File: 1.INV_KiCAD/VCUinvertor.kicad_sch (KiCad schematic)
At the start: 119 parts, among them J7 PowerSupply, J9 BRAKE LIGHT, Q1 2N7002, Q10 2N7002, Q11 BC848C, Q12 BCP51, Q2 2N7002, Q3 2N7002, Q4 2N7002, Q5 2N7002, Q6 2N7002, Q7 2N7002, Q8 2N7002, Q9 2N7002, U1 TJA1448ATK, U2 REF3433T, U3 TLV76150DCY

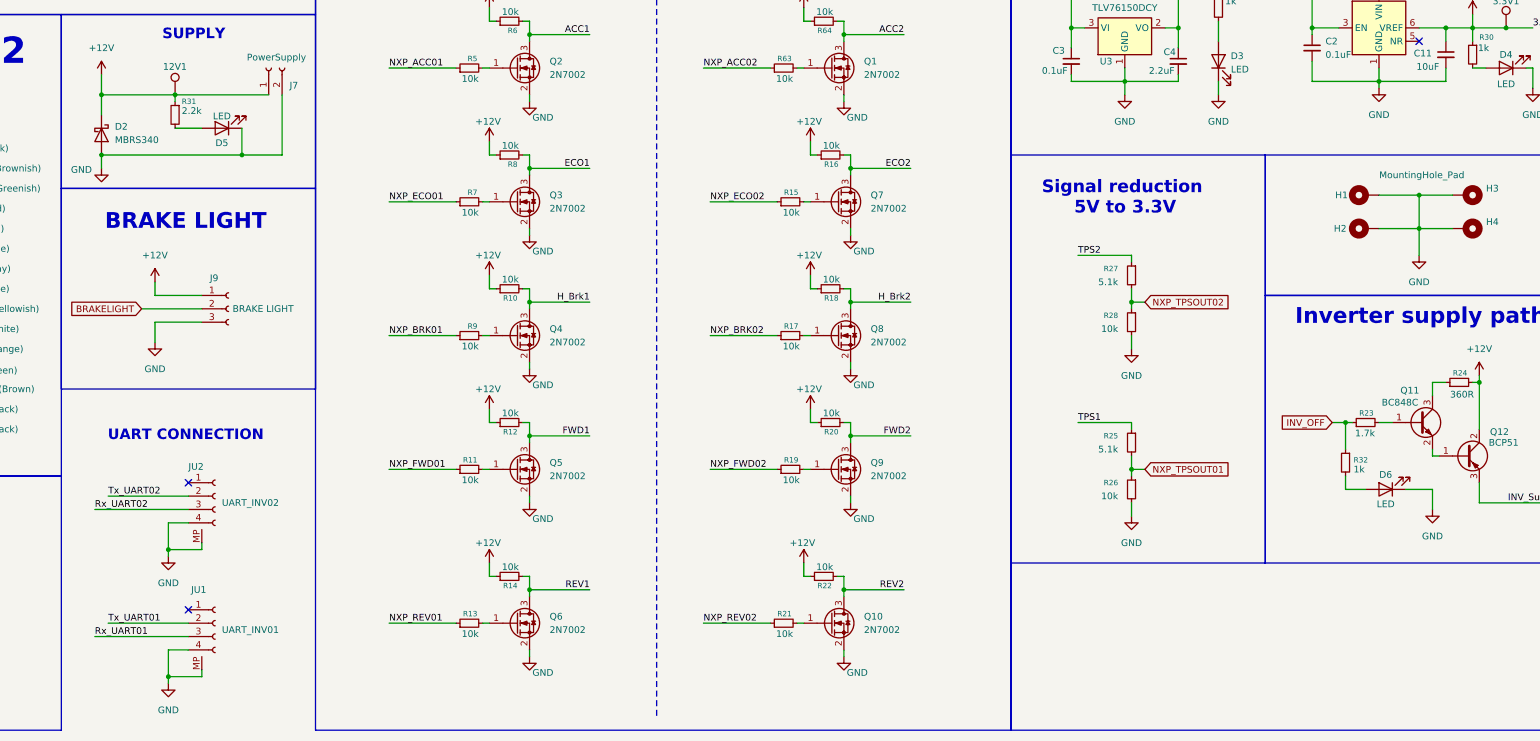
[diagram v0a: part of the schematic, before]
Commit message: Corrections on UART01/02
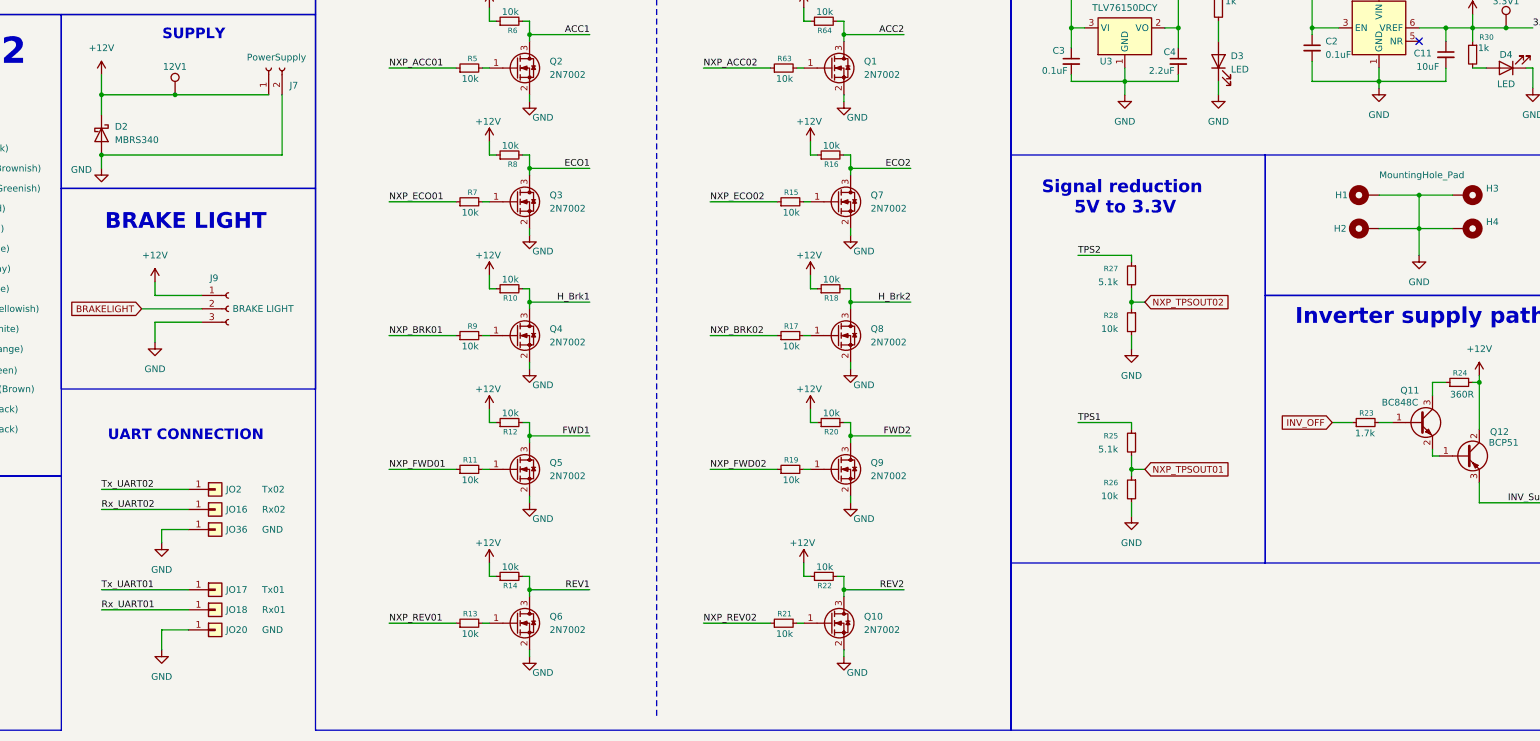
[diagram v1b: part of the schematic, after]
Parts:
- removed D5, D6: LED, LED_SMD:LED_0805_2012Metric_Pad1.15x1.40mm_HandSolder, symbol Device:LED
- removed JU1: UART_INV01, Connector_JST:JST_GH_SM04B-GHS-TB_1x04-1MP_P1.25mm_Horizontal, symbol Connector:Conn_01x04_Socket
- removed JU2: UART_INV02, Connector_JST:JST_GH_SM04B-GHS-TB_1x04-1MP_P1.25mm_Horizontal, symbol Connector:Conn_01x04_Socket
- removed R31: 2.2k, Resistor_SMD:R_0805_2012Metric, symbol Device:R_Small
- removed R32: 1k, Resistor_SMD:R_0805_2012Metric, symbol Device:R_Small
- added JO16: Rx02, Connector_Wire:SolderWire-0.5sqmm_1x01_D0.9mm_OD2.1mm, symbol Connector_Generic:Conn_01x01
- added JO17: Tx01, Connector_Wire:SolderWire-0.5sqmm_1x01_D0.9mm_OD2.1mm, symbol Connector_Generic:Conn_01x01
- added JO18: Rx01, Connector_Wire:SolderWire-0.5sqmm_1x01_D0.9mm_OD2.1mm, symbol Connector_Generic:Conn_01x01
- added JO2: Tx02, Connector_Wire:SolderWire-0.5sqmm_1x01_D0.9mm_OD2.1mm, symbol Connector_Generic:Conn_01x01
- added JO20, JO36: GND, Connector_Wire:SolderWire-0.5sqmm_1x01_D0.9mm_OD2.1mm, symbol Connector_Generic:Conn_01x01
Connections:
- net GND: now also JO20.1 (Pin_1), JO36.1 (Pin_1)
- net Rx_UART01: now also JO18.1 (Pin_1)
- net Rx_UART02: now also JO16.1 (Pin_1)
- net Tx_UART01: now also JO17.1 (Pin_1)
- net Tx_UART02: now also JO2.1 (Pin_1)
- no-connect marks 90 -> 88

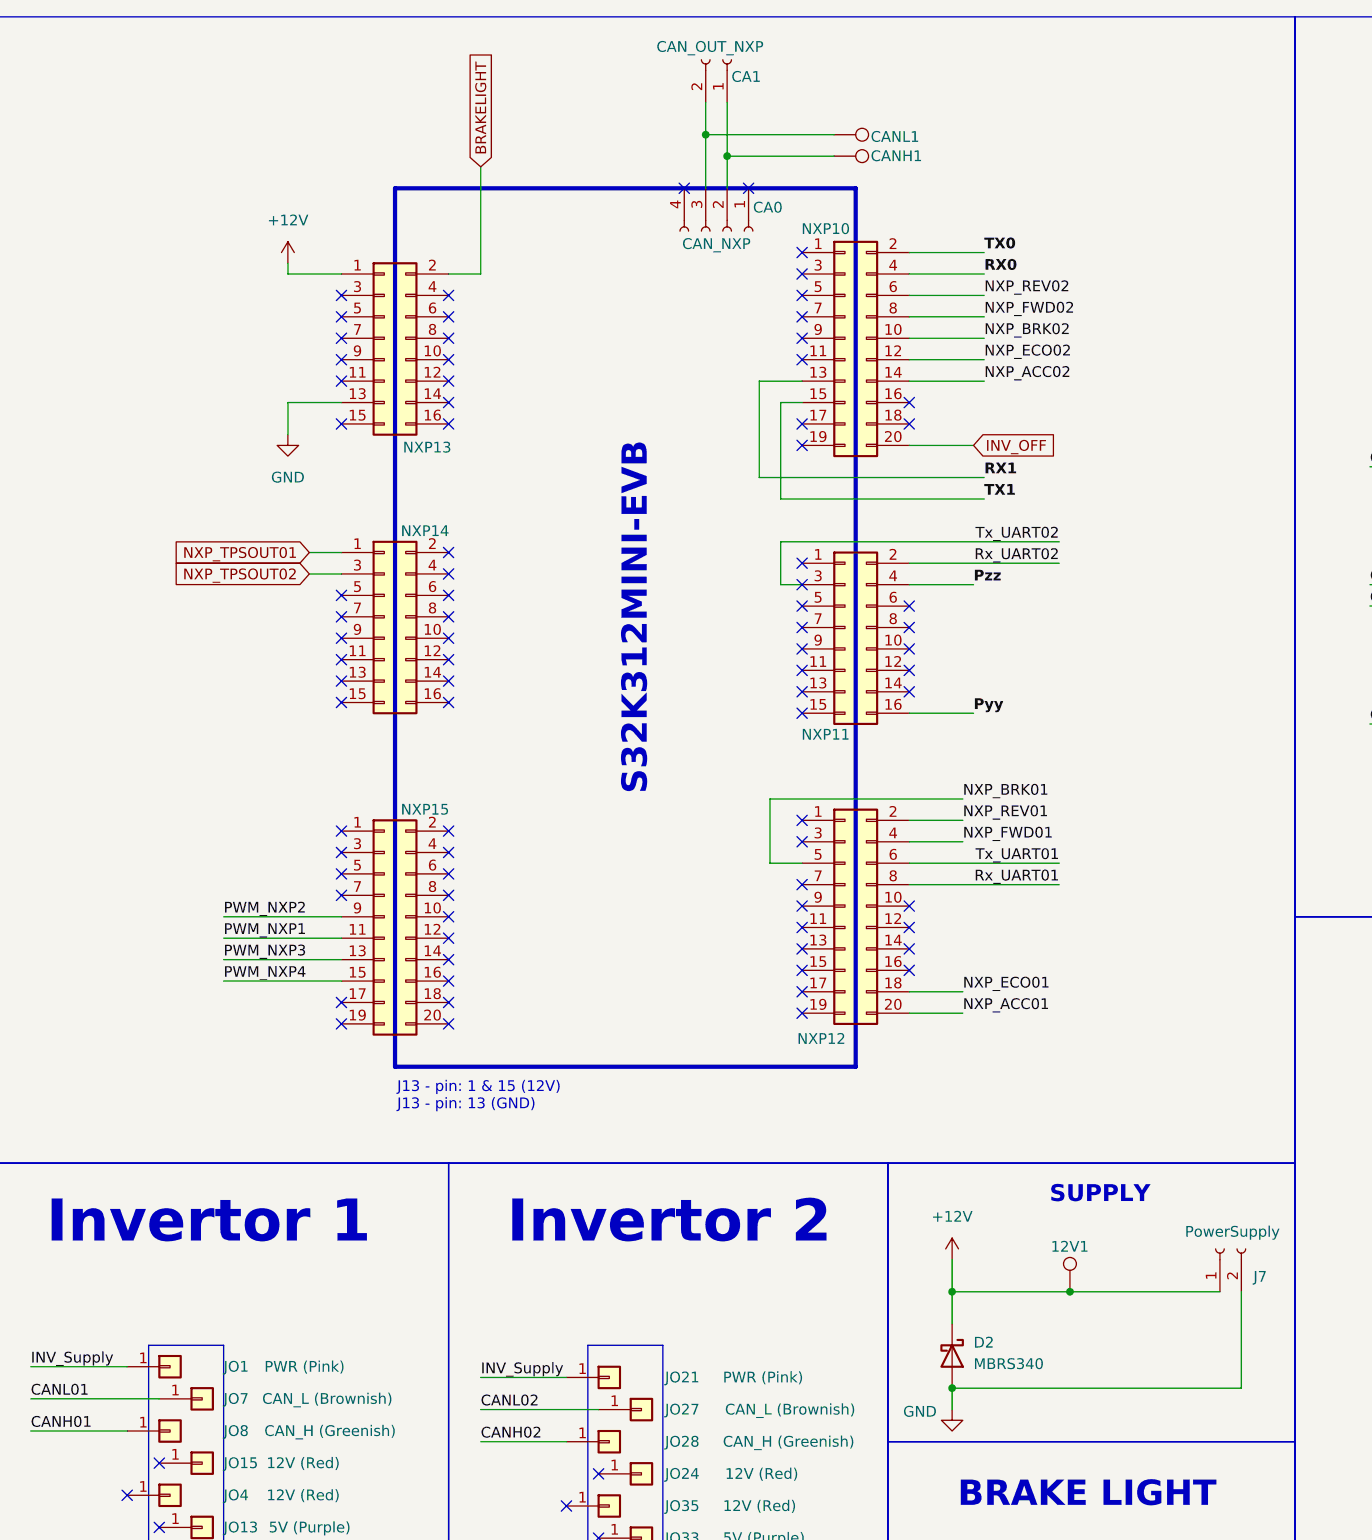
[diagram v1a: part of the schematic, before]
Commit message: Board - resized + Hole corrections
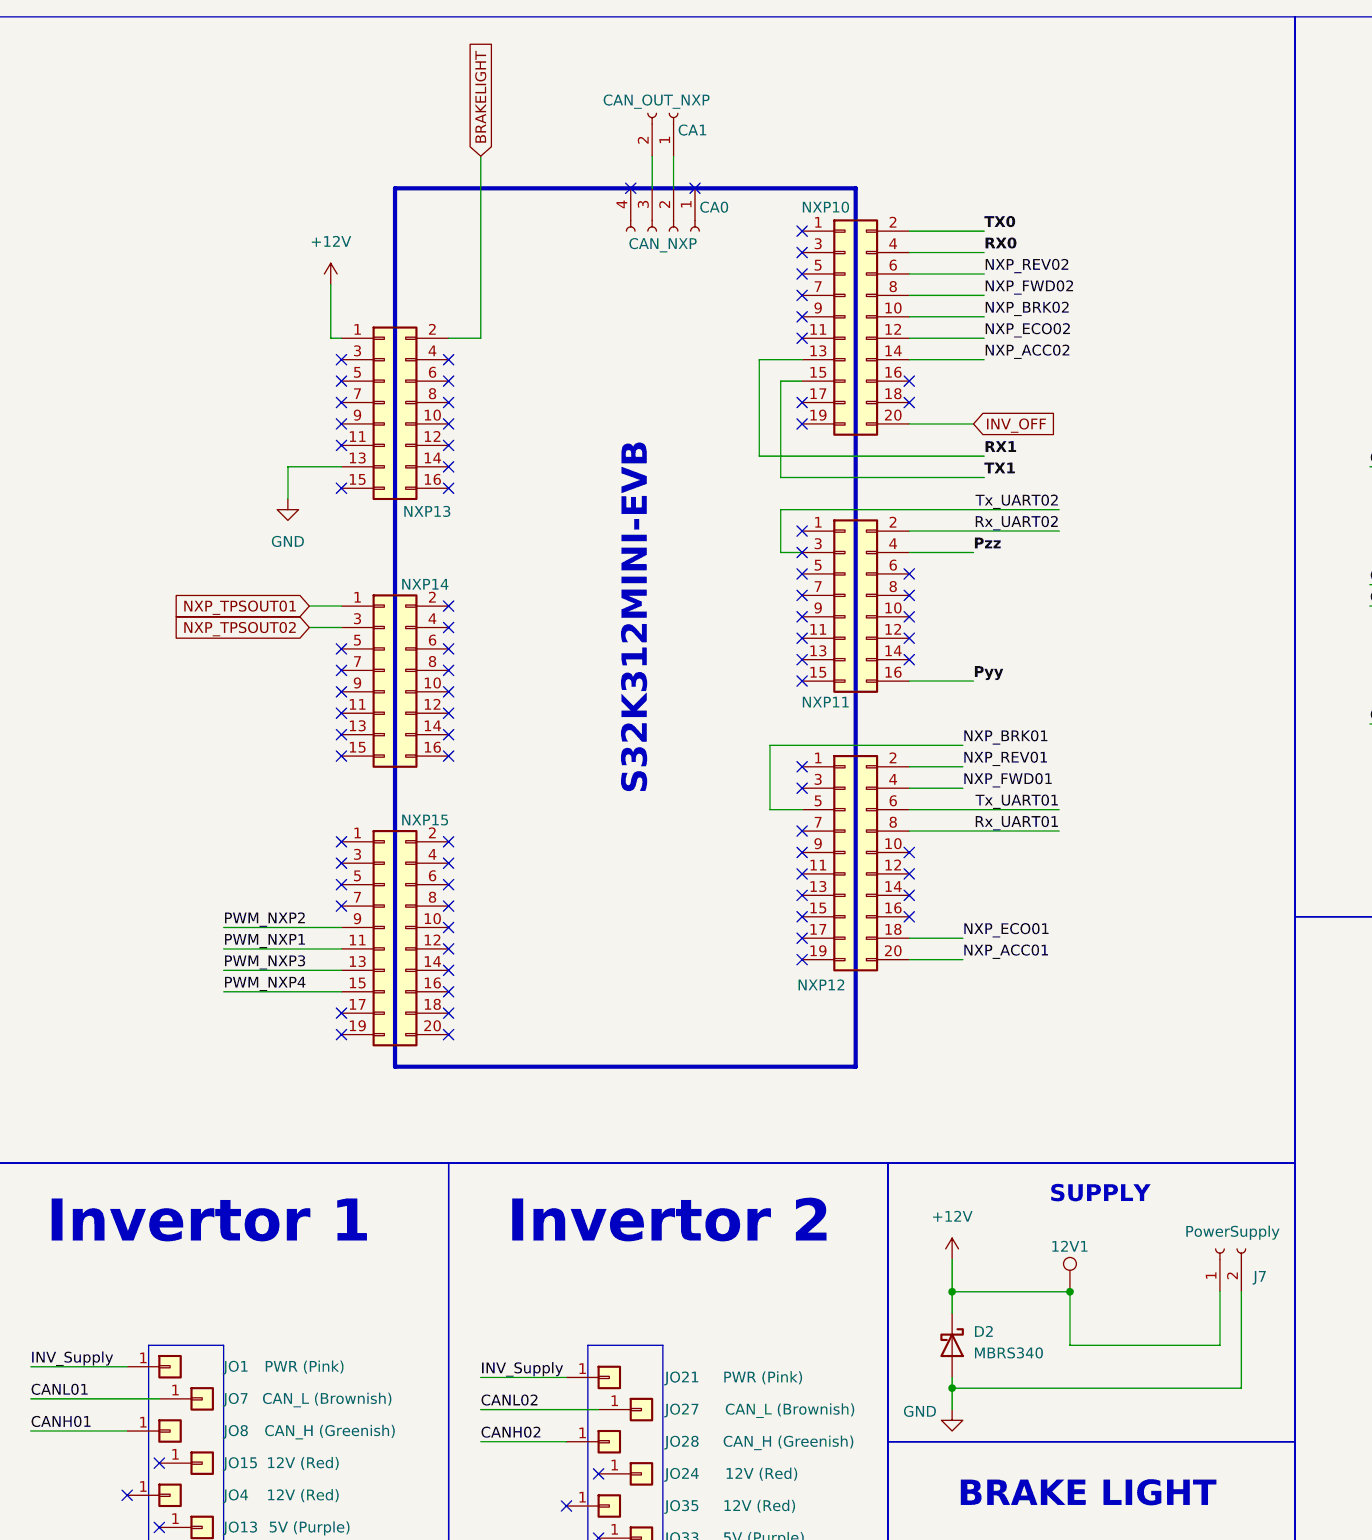
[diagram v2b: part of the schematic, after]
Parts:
- removed CANH1: CANH, TestPoint:TestPoint_Pad_D1.5mm, symbol Connector:TestPoint
- removed CANL1: CANL, TestPoint:TestPoint_Pad_D1.5mm, symbol Connector:TestPoint
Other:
- note removed: "J13 - pin: 1 & 15 (12V) J13 - pin: 13 (GND)"
- moved on the sheet: CA0, CA1, D2

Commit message: Redid layout for CAN and DAC chips
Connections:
- net Brk_AN2: now also DAC1.3 (VOUTB); no longer DAC1.2 (VOUTA)
- net PWM_NXP1: now also DAC1.5 (INB); no longer DAC1.6 (INA)
- net PWM_NXP2: now also DAC1.6 (INA); no longer DAC1.5 (INB)
- net PWM_NXP3: now also DAC1.10 (IND); no longer DAC1.11 (INC)
- net PWM_NXP4: now also DAC1.11 (INC); no longer DAC1.10 (IND)
- net RX0: now also U1.7 (RXD2); no longer U1.4 (RXD1)
- net RX1: now also U1.4 (RXD1); no longer U1.7 (RXD2)
- net TPS2: now also DAC1.2 (VOUTA); no longer DAC1.3 (VOUTB)
- net TX0: now also U1.6 (TXD2); no longer U1.1 (TXD1)
- net TX1: now also U1.1 (TXD1); no longer U1.6 (TXD2)

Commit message: CleanUp after changes
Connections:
- net NXP_ACC01: now also NXP12.7 (Pin_7); no longer NXP12.20 (Pin_20)
- net NXP_ACC02: now also NXP12.20 (Pin_20); no longer NXP10.14 (Pin_14)
- net NXP_BRK01: now also NXP12.4 (Pin_4); no longer NXP12.5 (Pin_5)
- net NXP_BRK02: now also NXP12.14 (Pin_14); no longer NXP10.10 (Pin_10)
- net NXP_ECO01: now also NXP12.5 (Pin_5); no longer NXP12.18 (Pin_18)
- net NXP_ECO02: now also NXP12.13 (Pin_13); no longer NXP10.12 (Pin_12)
- net NXP_FWD01: now also NXP12.3 (Pin_3); no longer NXP12.4 (Pin_4)
- net NXP_FWD02: now also NXP12.11 (Pin_11); no longer NXP10.8 (Pin_8)
- net NXP_REV02: now also NXP12.9 (Pin_9); no longer NXP10.6 (Pin_6)
- net Pyy: now also NXP10.18 (Pin_18); no longer NXP11.16 (Pin_16)
- net Pzz: now also NXP10.10 (Pin_10); no longer NXP11.4 (Pin_4)

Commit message: 12V -> BAT+
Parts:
- renumbered 12V1 to VCC_BAT1
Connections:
- net 12V_INV: now reaches JO24.1 (Pin_1)
- net 12V_INV: now also JO15.1 (Pin_1), JO35.1 (Pin_1), JO4.1 (Pin_1), R10.1, R12.1, R14.1, R16.1, R18.1, R20.1, R22.1, R6.1, R64.1, R8.1
- net +12V renamed BAT+
- net BAT+: no longer R10.1, R12.1, R14.1, R16.1, R18.1, R20.1, R22.1, R6.1, R64.1, R8.1
- no-connect marks 88 -> 84

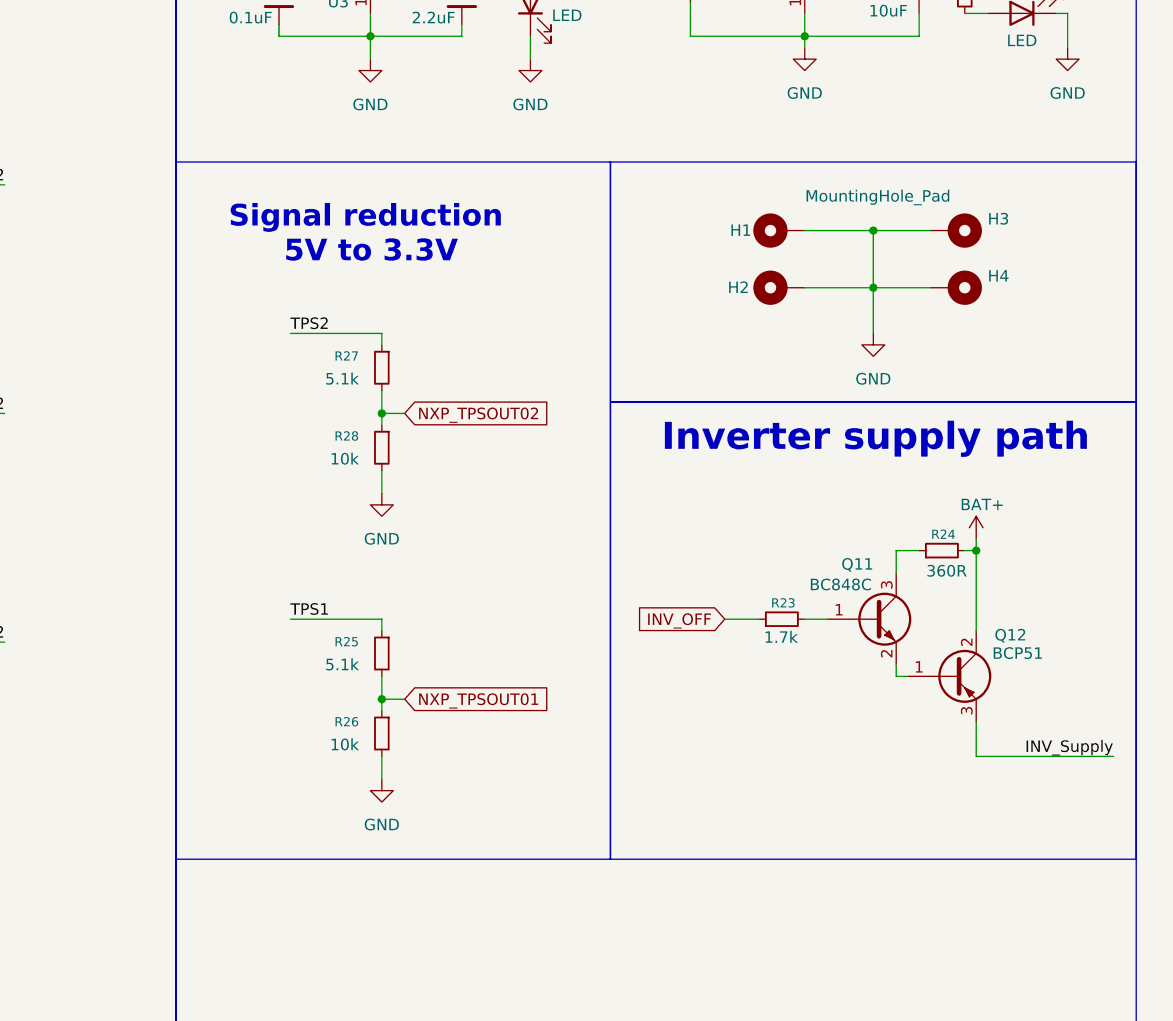
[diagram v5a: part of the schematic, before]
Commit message: Dorlington -> Relay for INV_OFF
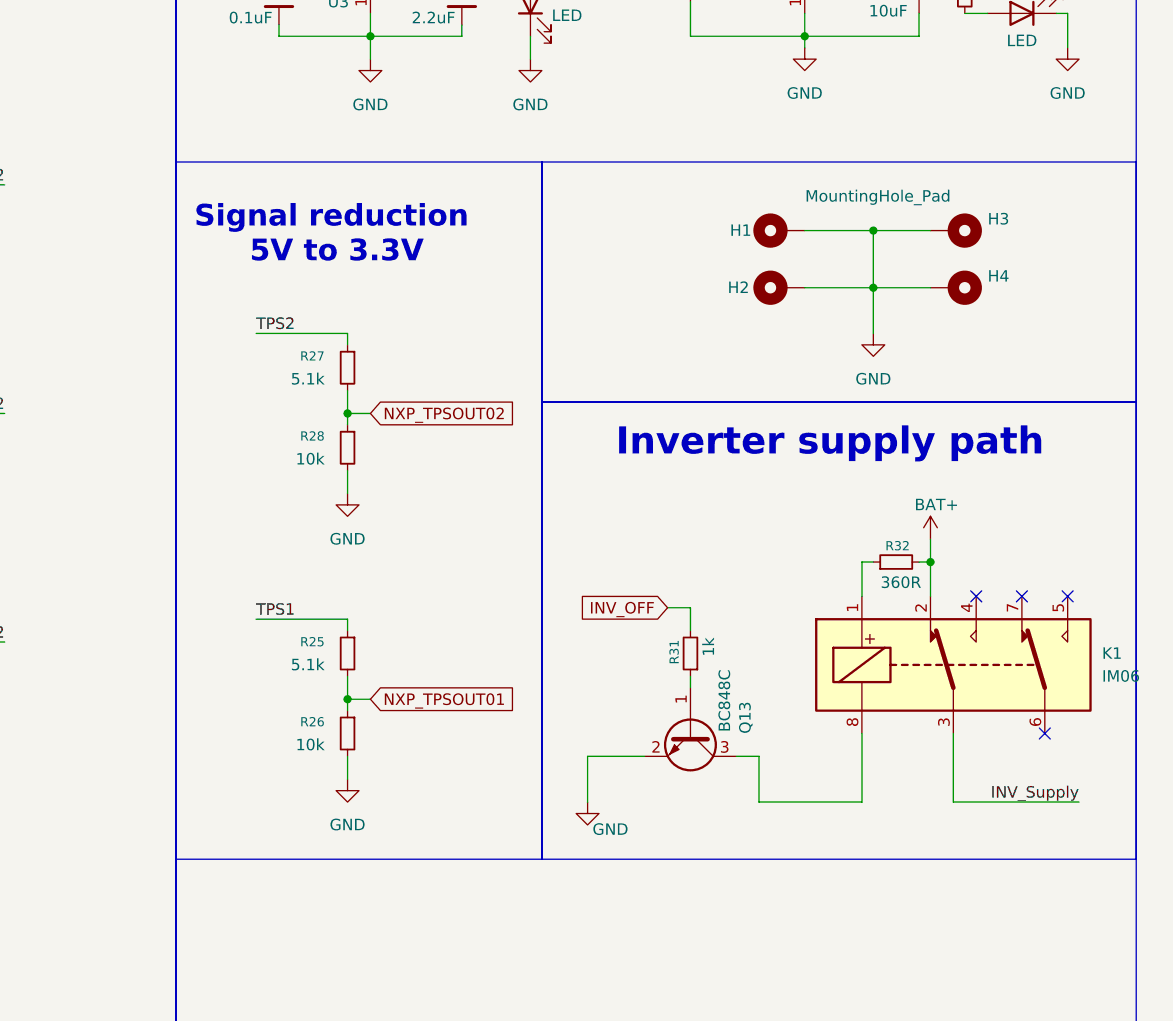
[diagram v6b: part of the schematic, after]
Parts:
- removed Q11: BC848C, Package_TO_SOT_SMD:SOT-23, symbol Transistor_BJT:BC848
- removed Q12: BCP51, Package_TO_SOT_SMD:SOT-223-3_TabPin2, symbol Transistor_BJT:BCP51
- removed R23: 1.7k, Resistor_SMD:R_1206_3216Metric_Pad1.30x1.75mm_HandSolder, symbol Device:R_Small
- removed R24: 360R, Resistor_SMD:R_1206_3216Metric_Pad1.30x1.75mm_HandSolder, symbol Device:R_Small
- added K1: IM06, Library_GHST:Relay_IM06DGR, symbol Relay:IM06
- added Q13: BC848C, Package_TO_SOT_SMD:SOT-23, symbol Transistor_BJT:BC848
- added R31: 1k, Resistor_SMD:R_1206_3216Metric_Pad1.30x1.75mm_HandSolder, symbol Device:R_Small
- added R32: 360R, Resistor_SMD:R_1206_3216Metric_Pad1.30x1.75mm_HandSolder, symbol Device:R_Small
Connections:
- net BAT+: now also K1.2, R32.2
- net GND: now also Q13.2 (E)
- net INV_OFF: now also R31.2
- net INV_Supply: now also K1.3
- new net: Q13.1 (B), R31.1
- new net: K1.8, Q13.3 (C)
- new net: K1.1, R32.1
- no-connect marks 84 -> 88
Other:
- moved on the sheet: R25, R26, R27, R28
